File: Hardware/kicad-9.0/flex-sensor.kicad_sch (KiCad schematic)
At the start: 0 parts

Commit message: Added: designed the first version of the schematic
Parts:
- added BMS1: BMS-1s, symbol BMS_Module:BMS-1s
- added BT1: Battery_Cell, symbol Device:Battery_Cell
- added C1, C2, C3, C4, C5, C6: 100n, symbol Device:C
- added R1, R2, R3, R4, R5: 30k, symbol Device:R
- added R6, R7: 100k, symbol Device:R
- added U1: XIAO-ESP32-S3, symbol MCU_XIAO:XIAO-ESP32-S3
- added U2, U3, U4, U5, U6: Sparkfun Flex Sensor, symbol Sensor_Flex:SparkFun-FlexSensor
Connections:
- new net: C1.2, C2.2, C3.2, C4.2, C5.2, U1.13 (GND)
- new net: BMS1.2 (P-), C6.2, R7.1, U1.16 (BAT-)
- new net: BMS1.3 (B-), BT1.2 (-)
- new net: BMS1.4 (B+), BT1.1 (+)
- new net: U1.12 (3V3), U2.1 (PIN_1), U3.1 (PIN_1), U4.1 (PIN_1), U5.1 (PIN_1), U6.1 (PIN_1)
- new net: R2.2, U3.2 (PIN_2)
- new net: C6.1, R6.2, R7.2
- new net: R5.2, U6.2 (PIN_2)
- new net: R4.2, U5.2 (PIN_2)
- new net: R3.2, U4.2 (PIN_2)
- new net: R1.2, U2.2 (PIN_2)
- new net BAT_LV: BMS1.1 (P+), R6.1, U1.10 (D9), U1.15 (BAT+)
- new net SENS1: C1.1, R1.1, U1.2 (D1)
- new net SENS2: C2.1, R2.1, U1.4 (D3)
- new net SENS3: C3.1, R3.1, U1.5 (D4)
- new net SENS4: C4.1, R4.1, U1.6 (D5)
- new net SENS5: C5.1, R5.1, U1.9 (D8)
- no-connect marks 0 -> 6

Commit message: FIX: moved the BAT_LV label to the correct position
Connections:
- net BAT_LV: now also C6.1, R6.2, R7.2; no longer BMS1.1 (P+), R6.1, U1.15 (BAT+)
- new net: BMS1.1 (P+), R6.1, U1.15 (BAT+)
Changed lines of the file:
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@@
-	)
-	(junction
-		(at 107.95 74.93)
-		(diameter 0)
-		(color 0 0 0 0)
 	)
 	(junction
@@
 	(wire
 		(pts
-			(xy 107.95 74.93) (xy 107.95 76.2)
+			(xy 107.95 72.39) (xy 107.95 76.2)
 		)
 		(stroke
@@
 	(wire
 		(pts
-			(xy 107.95 74.93) (xy 120.65 74.93)
-		)
-		(stroke
-			(width 0)
-			(type default)
-		)
-	)
-	(wire
-		(pts
 			(xy 144.78 110.49) (xy 152.4 110.49)
 		)
@@
 	(wire
 		(pts
+			(xy 107.95 86.36) (xy 120.65 86.36)
+		)
+		(stroke
+			(width 0)
+			(type default)
+		)
+	)
+	(wire
+		(pts
 			(xy 142.24 115.57) (xy 152.4 115.57)
 		)
@@
 		(pts
 			(xy 93.98 101.6) (xy 101.6 101.6)
-		)
-		(stroke
-			(width 0)
-			(type default)
-		)
-	)
-	(wire
-		(pts
-			(xy 107.95 72.39) (xy 107.95 74.93)
 		)
 		(stroke
@@
 		)
 	)
-	(label "BAT_LV"
-		(at 120.65 74.93 180)
-		(effects
-			(font
-				(size 1.27 1.27)
-			)
-			(justify right bottom)
-		)
-	)
 	(label "SENS5"
 		(at 120.65 53.34 180)
@@
 		)
 	)
+	(label "BAT_LV"
+		(at 120.65 86.36 180)
+		(effects
+			(font
+				(size 1.27 1.27)
+			)
+			(justify right bottom)
+		)
+	)

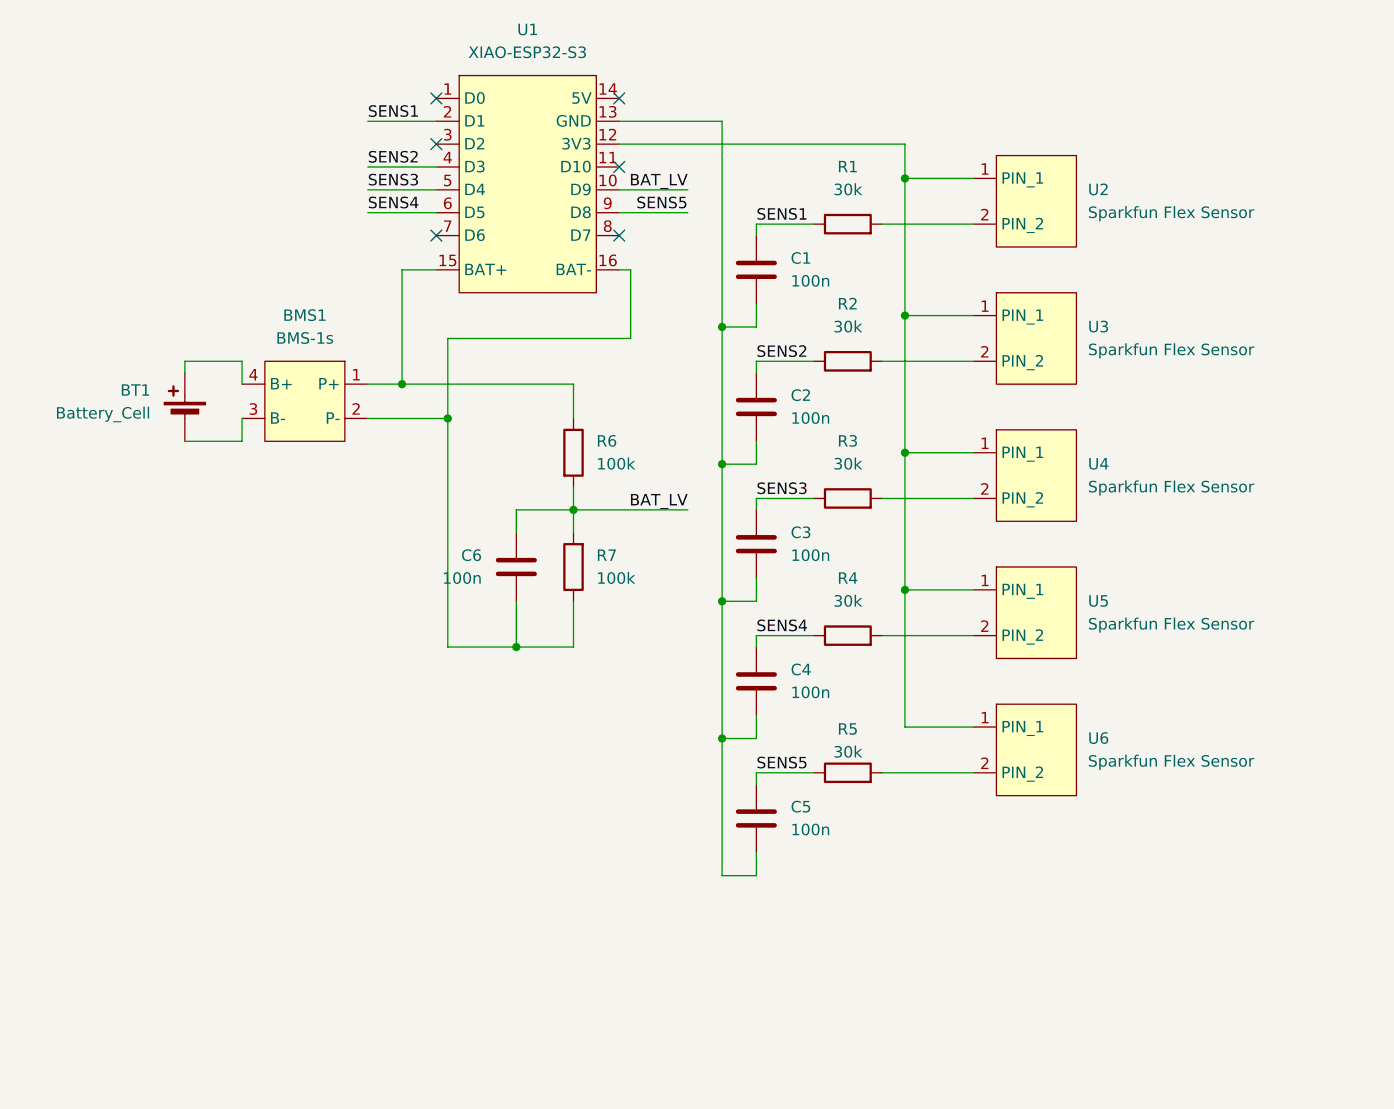
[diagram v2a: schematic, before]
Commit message: FIX: corrected the wiring of voltage dividers
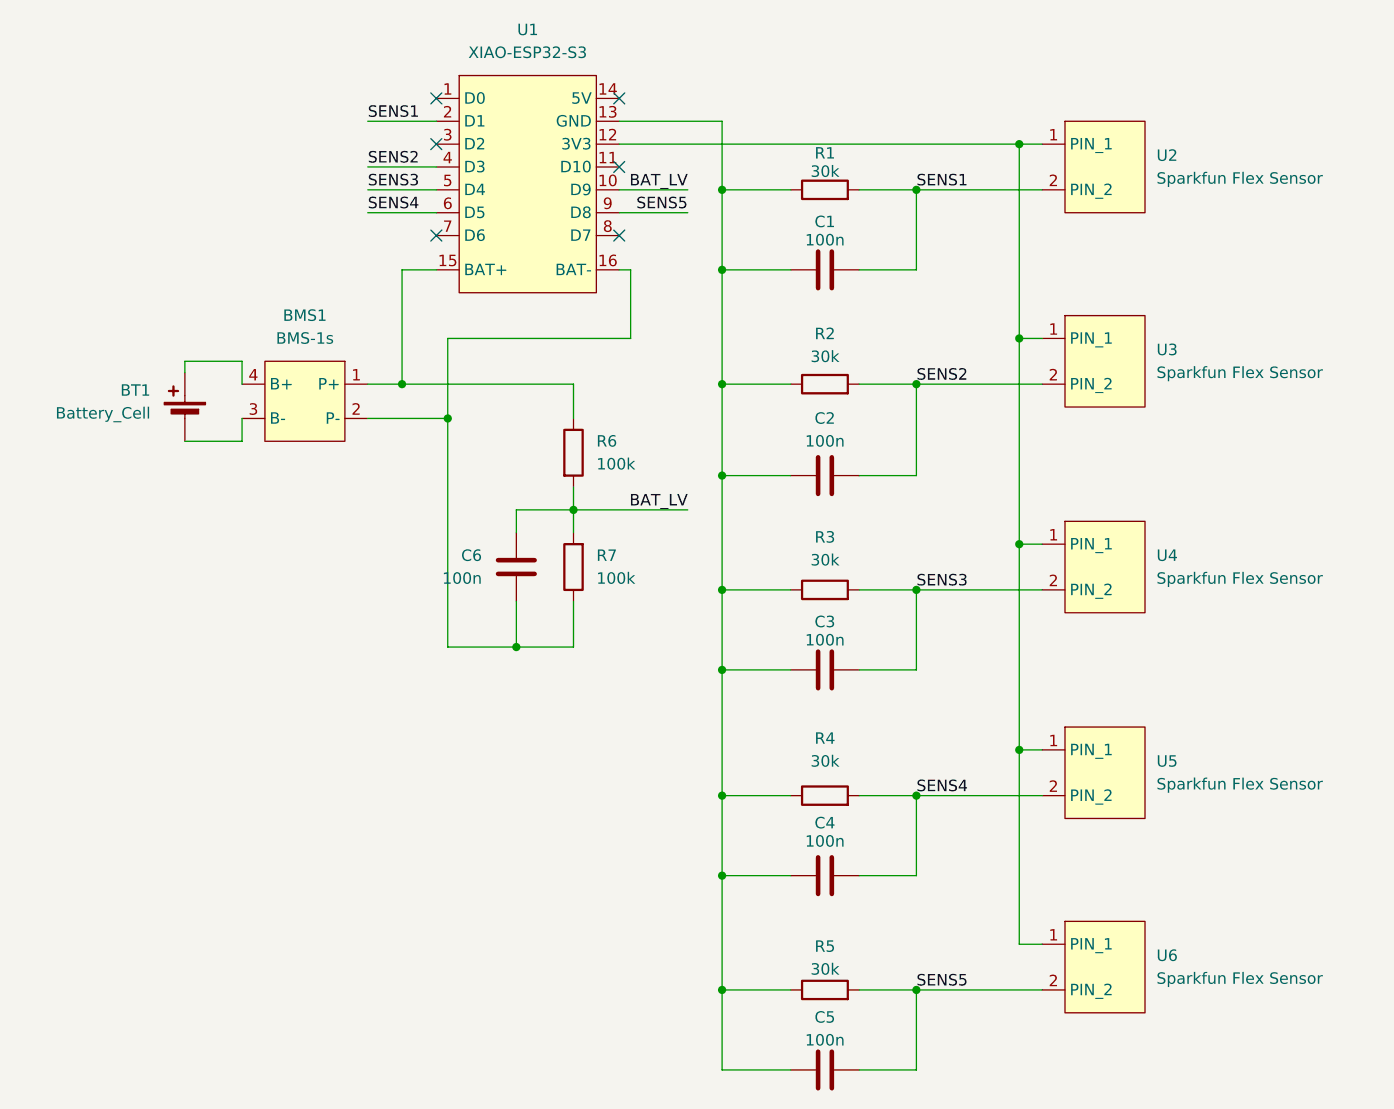
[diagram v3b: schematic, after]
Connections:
- net SENS1: now also C1.2, R1.2, U2.2 (PIN_2); no longer C1.1, R1.1
- net SENS2: now also C2.2, R2.2, U3.2 (PIN_2); no longer C2.1, R2.1
- net SENS3: now also C3.2, R3.2, U4.2 (PIN_2); no longer C3.1, R3.1
- net SENS4: now also C4.2, R4.2, U5.2 (PIN_2); no longer C4.1, R4.1
- net SENS5: now also C5.2, R5.2, U6.2 (PIN_2); no longer C5.1, R5.1
- new net: C1.1, C2.1, C3.1, C4.1, C5.1, R1.1, R2.1, R3.1, R4.1, R5.1, U1.13 (GND)
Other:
- moved on the sheet: C1, C2, C3, C4, C5, R1, R2, R3, R4, R5, U2, U3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
